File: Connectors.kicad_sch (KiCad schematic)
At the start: 4 parts, among them J1 Conn_01x04_Pin, J2 Conn_01x04_Pin, J3 Conn_01x09_Pin, J4 Conn_02x03_Odd_Even

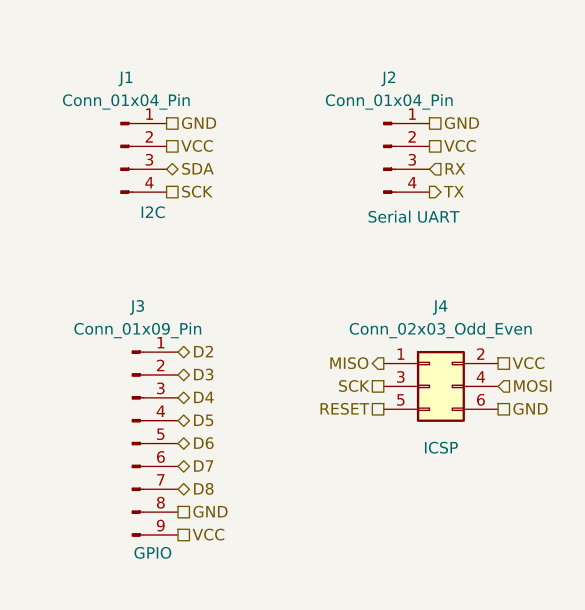
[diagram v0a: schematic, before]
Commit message: Fixed two defects in the schematics
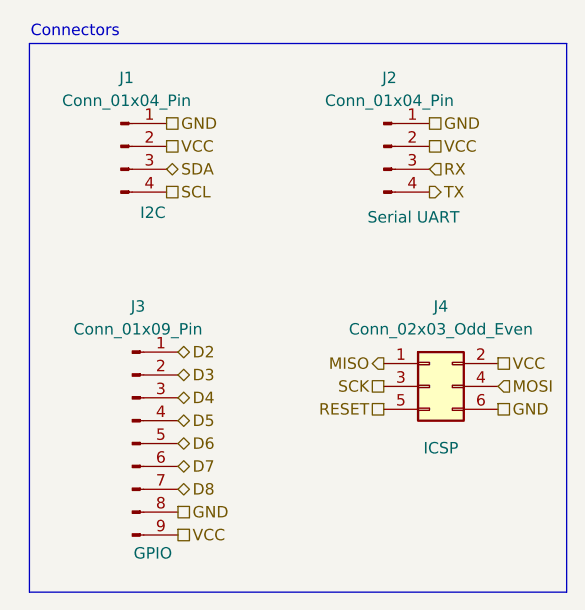
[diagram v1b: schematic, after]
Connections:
- net SCK: no longer J1.4 (Pin_4)
- new net SCL: J1.4 (Pin_4)
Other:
- note added: "Connectors"
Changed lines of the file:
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@@
 	(generator_version "10.0")
 	(paper "A4")
+	(text "Connectors\n"
+		(exclude_from_sim no)
+		(at 106.68 82.55 0)
+		(effects
+			(font
+				(size 1.27 1.27)
+			)
+		)
+	)
+	(polyline
+		(pts
+			(xy 101.6 83.82) (xy 101.6 144.78)
+		)
+		(stroke
+			(width 0)
+			(type default)
+		)
+	)
+	(polyline
+		(pts
+			(xy 161.29 144.78) (xy 101.6 144.78)
+		)
+		(stroke
+			(width 0)
+			(type default)
+		)
+	)
+	(polyline
+		(pts
+			(xy 101.6 83.82) (xy 161.29 83.82)
+		)
+		(stroke
+			(width 0)
+			(type default)
+		)
+	)
+	(polyline
+		(pts
+			(xy 161.29 83.82) (xy 161.29 144.78)
+		)
+		(stroke
+			(width 0)
+			(type default)
+		)
+	)
 	(hierarchical_label "SDA"
 		(shape bidirectional)
@@
 		)
 	)
-	(hierarchical_label "SCK"
+	(hierarchical_label "SCL"
 		(shape passive)
 		(at 116.84 100.33 0)
